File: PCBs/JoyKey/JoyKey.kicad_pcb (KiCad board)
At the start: 2 copper layers, 90.2 x 55 mm, 15 parts, among them J1 OLED_DISPLAY, SW2 SW_Push_45deg, SW3 SW_Push_45deg, SW4 SW_Push_45deg, SW5 SW_Push_45deg, U1 Seeed Studio XIAO RP2040

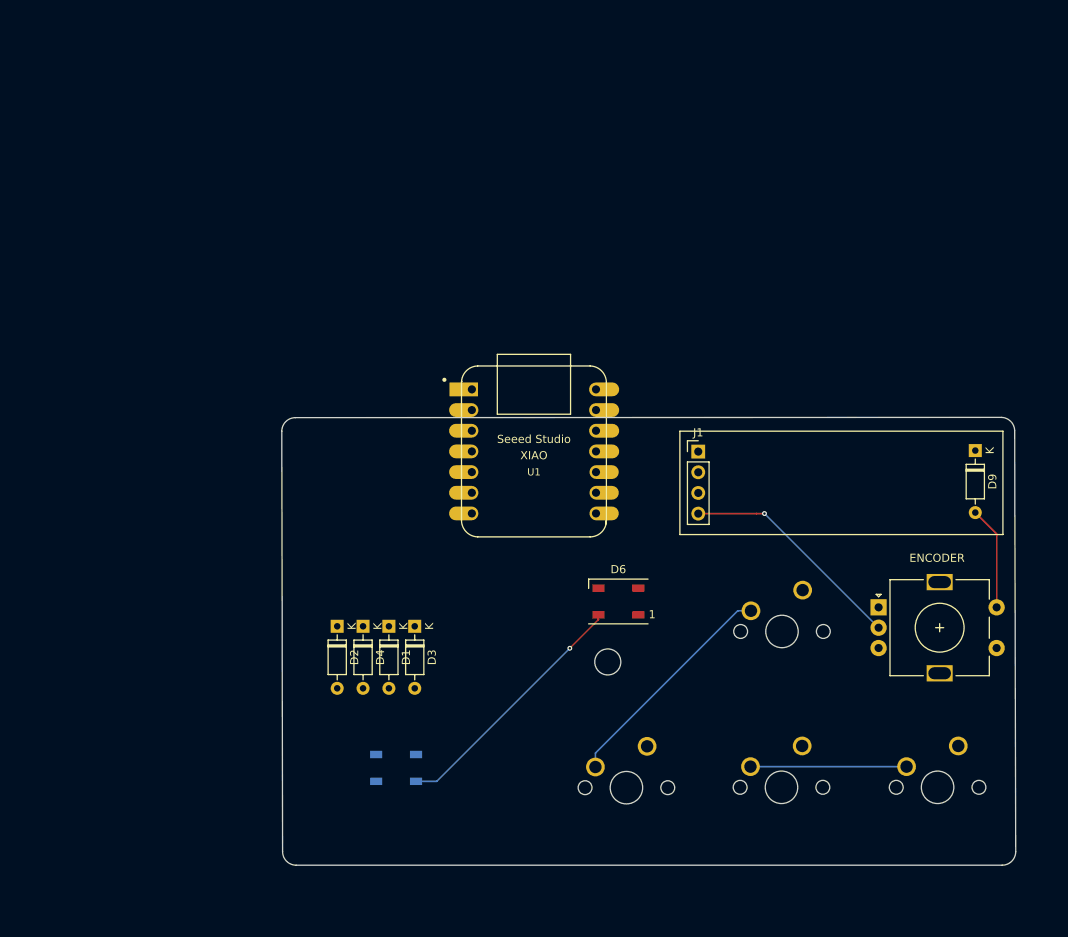
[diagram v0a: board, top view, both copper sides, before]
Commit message: Updated Parts in PCB
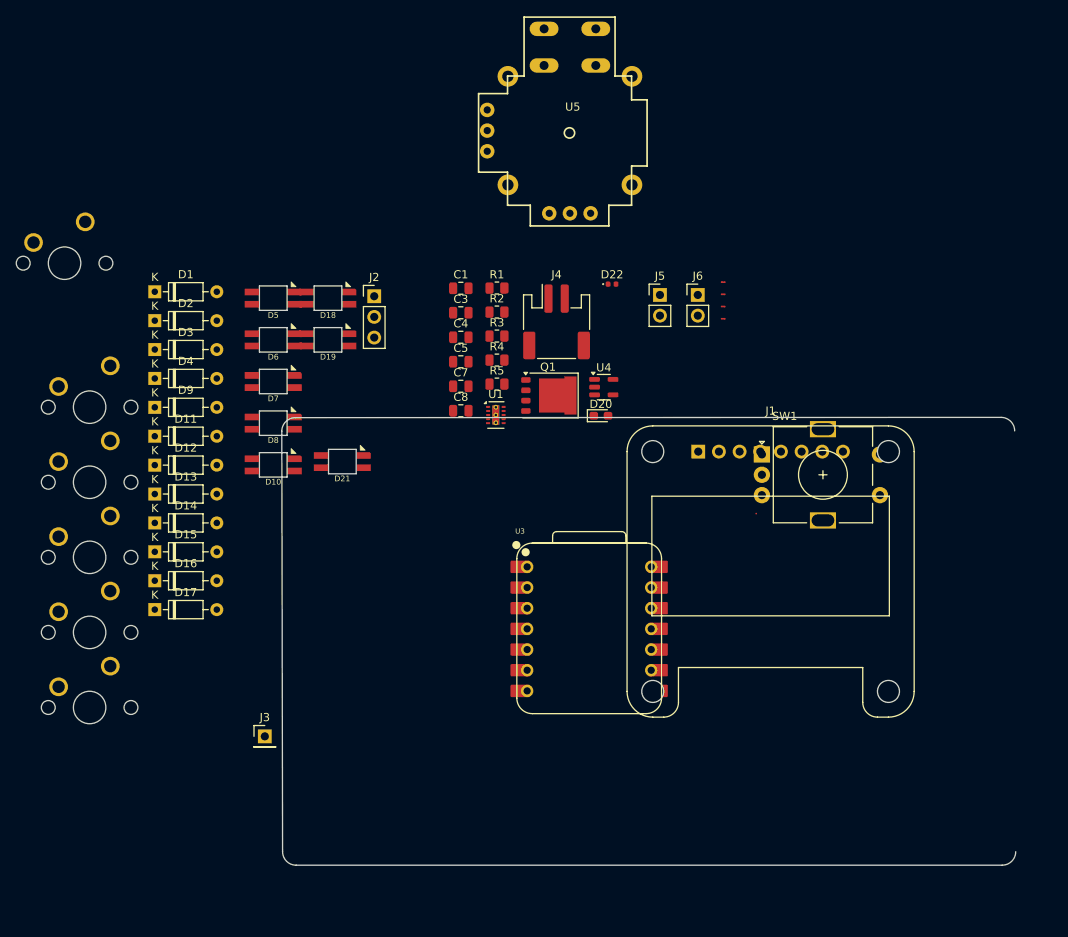
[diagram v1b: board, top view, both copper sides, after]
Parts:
- removed ENCODER: RotaryEncoder_Switch, Rotary_Encoder:RotaryEncoder_Alps_EC11E-Switch_Vertical_H20mm
- removed REF**: MountingHole_3.2mm_M3, MountingHole:MountingHole_3.2mm_M3
- added C1: 10uF, 16v, Capacitor_SMD:C_0805_2012Metric, F.Cu at (122.3, 58.2)
- added C3: 10uF, 16v, Capacitor_SMD:C_0805_2012Metric, F.Cu at (122.3, 61.2)
- added C4: 10uF, 16v, Capacitor_SMD:C_0805_2012Metric, F.Cu at (122.3, 64.2)
- added C5: 1uF, Capacitor_SMD:C_0805_2012Metric, F.Cu at (122.3, 67.2)
- added C7: 100nF, 16v, Capacitor_SMD:C_0805_2012Metric, F.Cu at (122.3, 70.2)
- added C8: 2.2uF, 10v, Capacitor_SMD:C_0805_2012Metric, F.Cu at (122.3, 73.2)
- added D10: SK6812MINI, SK6812MINI-E:SK6812MINI-E, F.Cu at (99.3, 79.9)
- added D11: D, Diode_THT:D_DO-35_SOD27_P7.62mm_Horizontal, F.Cu at (84.7, 76.3)
- added D12: D, Diode_THT:D_DO-35_SOD27_P7.62mm_Horizontal, F.Cu at (84.7, 79.9)
- added D13: D, Diode_THT:D_DO-35_SOD27_P7.62mm_Horizontal, F.Cu at (84.7, 83.4)
- added D14: D, Diode_THT:D_DO-35_SOD27_P7.62mm_Horizontal, F.Cu at (84.7, 87.0)
- added D15: D, Diode_THT:D_DO-35_SOD27_P7.62mm_Horizontal, F.Cu at (84.7, 90.5)
- added D16: D, Diode_THT:D_DO-35_SOD27_P7.62mm_Horizontal, F.Cu at (84.7, 94.1)
- added D17: D, Diode_THT:D_DO-35_SOD27_P7.62mm_Horizontal, F.Cu at (84.7, 97.6)
- added D18: SK6812MINI, SK6812MINI-E:SK6812MINI-E, F.Cu at (106.0, 59.4)
- added D19: SK6812MINI, SK6812MINI-E:SK6812MINI-E, F.Cu at (106.0, 64.5)
- added D20: Osram LT Q99G.01 green led, LED_SMD:LED_0603_1608Metric_Pad1.05x0.95mm_HandSolder, F.Cu at (139.6, 73.8)
- added D21: SK6812MINI, SK6812MINI-E:SK6812MINI-E, F.Cu at (107.8, 79.5)
- added D22: GSDH3005, Diode_SMD:D_0402_1005Metric, F.Cu at (140.9, 57.7)
- added D7: SK6812MINI, SK6812MINI-E:SK6812MINI-E, F.Cu at (99.3, 69.6)
- added D8: SK6812MINI, SK6812MINI-E:SK6812MINI-E, F.Cu at (99.3, 74.7)
- added J2: Conn_01x03_Socket, Connector_PinHeader_2.54mm:PinHeader_1x03_P2.54mm_Vertical, F.Cu at (111.7, 59.1)
- added J3: Testpad wire hole1, Connector_PinHeader_2.54mm:PinHeader_1x01_P2.54mm_Vertical, F.Cu at (98.3, 113.2)
- added J4: JST PH, Connector_JST:JST_PH_S2B-PH-SM4-TB_1x02-1MP_P2.00mm_Horizontal, F.Cu at (134.1, 62.3)
- added J5: Top Trigger 1, Connector_PinHeader_2.54mm:PinHeader_1x02_P2.54mm_Vertical, F.Cu at (146.8, 59.0)
- added J6: Top Trigger 2, Connector_PinHeader_2.54mm:PinHeader_1x02_P2.54mm_Vertical, F.Cu at (151.5, 59.0)
- added NT1: NetTie_2, custom_Connector:NetTie-2_SMD_Pad0.2mm, F.Cu at (154.6, 57.4)
- added NT2: NetTie_2, custom_Connector:NetTie-2_SMD_Pad0.2mm, F.Cu at (154.6, 58.9)
- added NT3: NetTie_2, custom_Connector:NetTie-2_SMD_Pad0.2mm, F.Cu at (154.6, 60.4)
- added NT4: NetTie_2, custom_Connector:NetTie-2_SMD_Pad0.2mm, F.Cu at (154.6, 61.9)
- added Q1: PMOS,Si7157DP, Package_DFN_QFN:PQFN-8-EP_6x5mm_P1.27mm_Generic, F.Cu at (133.1, 71.3)
- added R1: 402 ohm, Resistor_SMD:R_0805_2012Metric, F.Cu at (126.8, 58.1)
- added R2: 1k, Resistor_SMD:R_0805_2012Metric, F.Cu at (126.8, 61.1)
- added R3: 230ohm, Resistor_SMD:R_0805_2012Metric, F.Cu at (126.8, 64.0)
- added R4: 1k, Resistor_SMD:R_0805_2012Metric, F.Cu at (126.8, 67.0)
- added R5: 2k, Resistor_SMD:R_0805_2012Metric, F.Cu at (126.8, 69.9)
- added SW1: RotaryEncoder_Switch, Rotary_Encoder:RotaryEncoder_Alps_EC11E-Switch_Vertical_H20mm, F.Cu at (159.3, 78.6)
- added SW6: SW_Push_45deg, MX_Solderable:MX-Solderable-1U, F.Cu at (76.7, 100.4)
- added SW7: SW_Push_45deg, MX_Solderable:MX-Solderable-1U, F.Cu at (76.7, 109.7)
- added U3: XIAO-RP2040-DIP, SEEED_XIAO:XIAO-RP2040-DIP, F.Cu at (138.1, 100.0)
- added U4: LP2981-3.3, Package_TO_SOT_SMD:SOT-23-5, F.Cu at (139.9, 70.3)
- added U5: 2_axis_analog_joystick_button, custom_Interface_HID:Adafruit 2-Axis joystick, F.Cu at (135.7, 39.1)
- D5: value WS2812B -> SK6812MINI; footprint LED_SMD:LED_WS2812B_PLCC4_5.0x5.0mm_P3.2mm -> SK6812MINI-E:SK6812MINI-E; moved to F.Cu
- D6: value WS2812B -> SK6812MINI; footprint LED_SMD:LED_WS2812B_PLCC4_5.0x5.0mm_P3.2mm -> SK6812MINI-E:SK6812MINI-E
- J1: footprint Connector_PinHeader_2.54mm:PinHeader_1x04_P2.54mm_Vertical -> Display:Adafruit_SSD1306
- U1: value Seeed Studio XIAO RP2040 -> BQ25060; footprint Seeed Studio XIAO Series Library:XIAO-Generic-Hybrid-14P-2.54-21X17.8MM -> custom_Power:WSON-10-1EP_2x3mm_P0.5mm_EP0.84x2.4mm_ThermalVias_0.3mm
- moved SW5 107.9 mm to (76.7, 91.2)
- moved D9 100.9 mm to (84.7, 72.8), turned to 0 degrees
- moved SW2 99.1 mm to (73.7, 55.1)
- moved SW4 92.9 mm to (76.7, 82.0)
- moved SW3 80.8 mm to (76.7, 72.8)
- moved D5 59.7 mm to (99.3, 59.4), turned to 0 degrees
- moved D6 53.2 mm to (99.3, 64.5), turned to 0 degrees
- moved D1 50.2 mm to (84.7, 58.6), turned to 0 degrees
- moved D3 46.6 mm to (84.7, 65.7), turned to 0 degrees
- moved D2 43.7 mm to (84.7, 62.1), turned to 0 degrees
- moved D4 39.8 mm to (84.7, 69.2), turned to 0 degrees
- moved U1 6.47 mm to (126.6, 73.7)
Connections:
- D1 pad 1: ROW0 -> /ROW0
- D2 pad 1: ROW0 -> /ROW0
- D3 pad 1: ROW1 -> /ROW0
- D4 pad 1: ROW1 -> /ROW1
- D5 pad 1: VCC -> Net-(D5-DOUT)
- D5 pad 2: Net-(D5-DOUT) -> GND
- D5 pad 3: GND -> Net-(D21-DOUT)
- D5 pad 4: WS2812B -> +3V3
- D6 pad 1: VCC -> Net-(D6-DOUT)
- D6 pad 2: unconnected-(D6-DOUT-Pad2) -> GND
- D6 pad 3: GND -> Net-(D5-DOUT)
- D6 pad 4: Net-(D5-DOUT) -> +3V3
- D9 pad 1: ROW0 -> /ROW1
- D9 pad 2: EC11SWA -> Net-(D9-A)
- J1 pad 3: VCC -> +3V3
- SW2 pad 1: COL0 -> /COL0
- SW3 pad 1: COL0 -> /COL1
- SW3 pad 2: Net-(D3-A) -> Net-(D2-A)
- SW4 pad 1: COL1 -> /COL0
- SW5 pad 1: COL1 -> /COL1
- SW5 pad 2: Net-(D2-A) -> Net-(D9-A)
- U1 pad 1: COL1 -> VCC
- U1 pad 10: COL2 -> Net-(U1-OUT)
- U1 pad 11: WS2812B -> GND
- U1 pad 2: COL0 -> Net-(U1-ISET)
- U1 pad 3: ROW1 -> GND
- U1 pad 4: ROW0 -> /Battery Management/LDO 4.9v
- U1 pad 5: SDA -> Net-(U1-TS)
- U1 pad 6: SCL -> /Battery Management/BATT+
- U1 pad 7: unconnected-(U1-PB08_A6_D6_TX-Pad7) -> GND
- U1 pad 8: EC11B -> /Battery Management/~{CHG}
- U1 pad 9: EC11A -> Net-(Q1-G)
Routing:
- net Net-(D5-DOUT): track 31.2 -> 0.00 mm, vias 1 -> 0
- net COL0: track 28.1 -> 0.00 mm
- net GND: track 28.0 -> 0.01 mm, vias 1 -> 0
- net COL1: track 19.2 -> 0.00 mm
- net EC11SWA: track 12.8 -> 0.00 mm
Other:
- board text added: "5.08 LED offset from key center"

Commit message: Started pcb placement
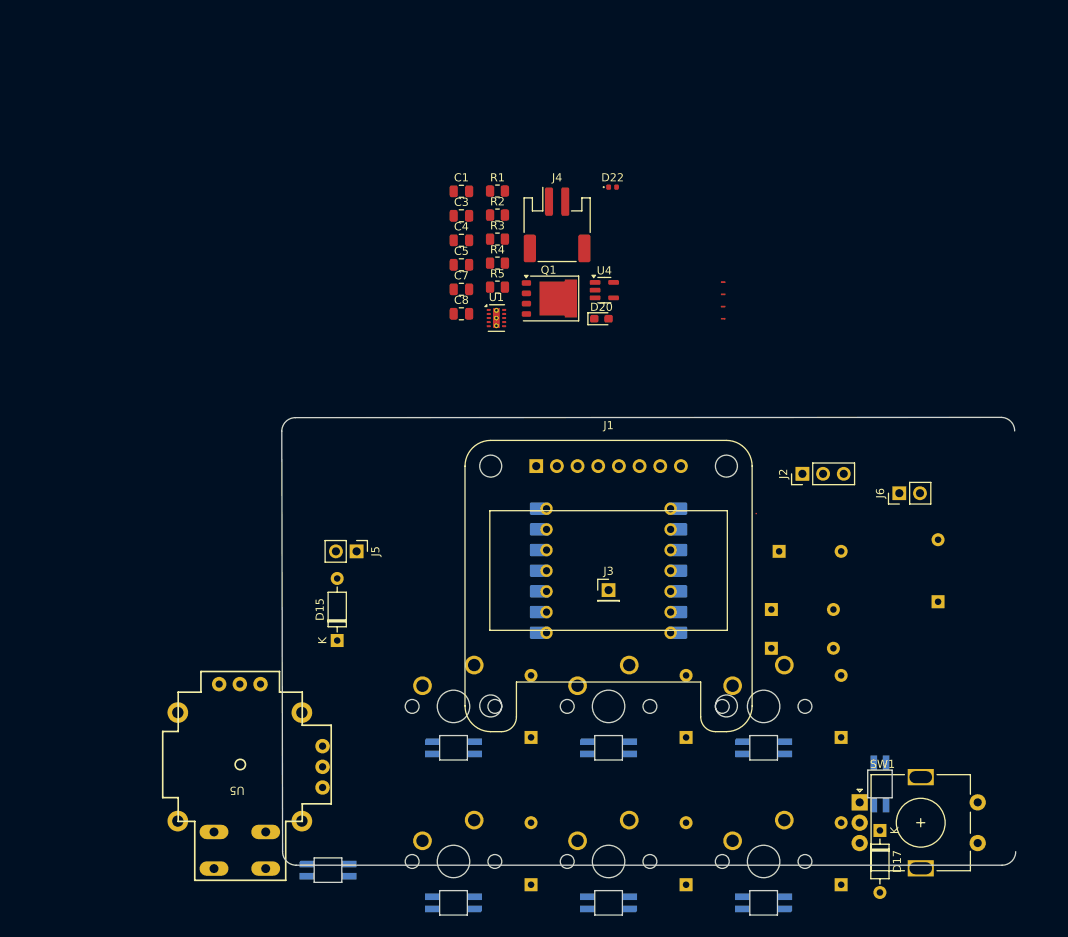
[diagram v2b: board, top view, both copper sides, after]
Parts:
- D1, D10, D11, D12, D13, D14, D16, D18, D19, D2, D21, D3, D4, D5, D6, D7, D8, D9, U3: moved to B.Cu
- moved D11 100.7 mm to (169.1, 131.4), turned to 90 degrees
- moved D3 96.9 mm to (169.1, 113.3), turned to 90 degrees
- moved D16 96.3 mm to (181.0, 96.7), turned to 90 degrees
- moved D17 93.1 mm to (173.8, 124.8), turned to -90 degrees
- moved D7 87.9 mm to (159.5, 133.7)
- moved D9 87.8 mm to (150.0, 131.4), turned to 90 degrees
- moved U5 87.5 mm to (95.2, 116.7), turned to 180 degrees
- moved SW6 87.5 mm to (159.5, 128.6)
- moved D19 87.0 mm to (173.8, 119.1), turned to -90 degrees
- moved D2 83.0 mm to (150.0, 113.3), turned to 90 degrees
- moved SW7 82.8 mm to (159.5, 109.5)
- moved D6 78.4 mm to (159.5, 114.6), turned to 180 degrees
- moved D4 77.5 mm to (131.0, 131.4), turned to 90 degrees
- moved D12 77.4 mm to (161.4, 90.5)
- moved D14 77.3 mm to (160.5, 102.4)
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
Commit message: Updated PCB components
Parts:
- moved D19 4.44 mm to (174.3, 114.7)
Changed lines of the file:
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@@
 	(footprint "SK6812MINI-E:SK6812MINI-E"
 		(layer "B.Cu")
-		(at 173.83125 119.0625 -90)
+		(at 174.3 114.65 -90)
 		(property "Reference" "D19"
 			(at 0 -2.1 90)

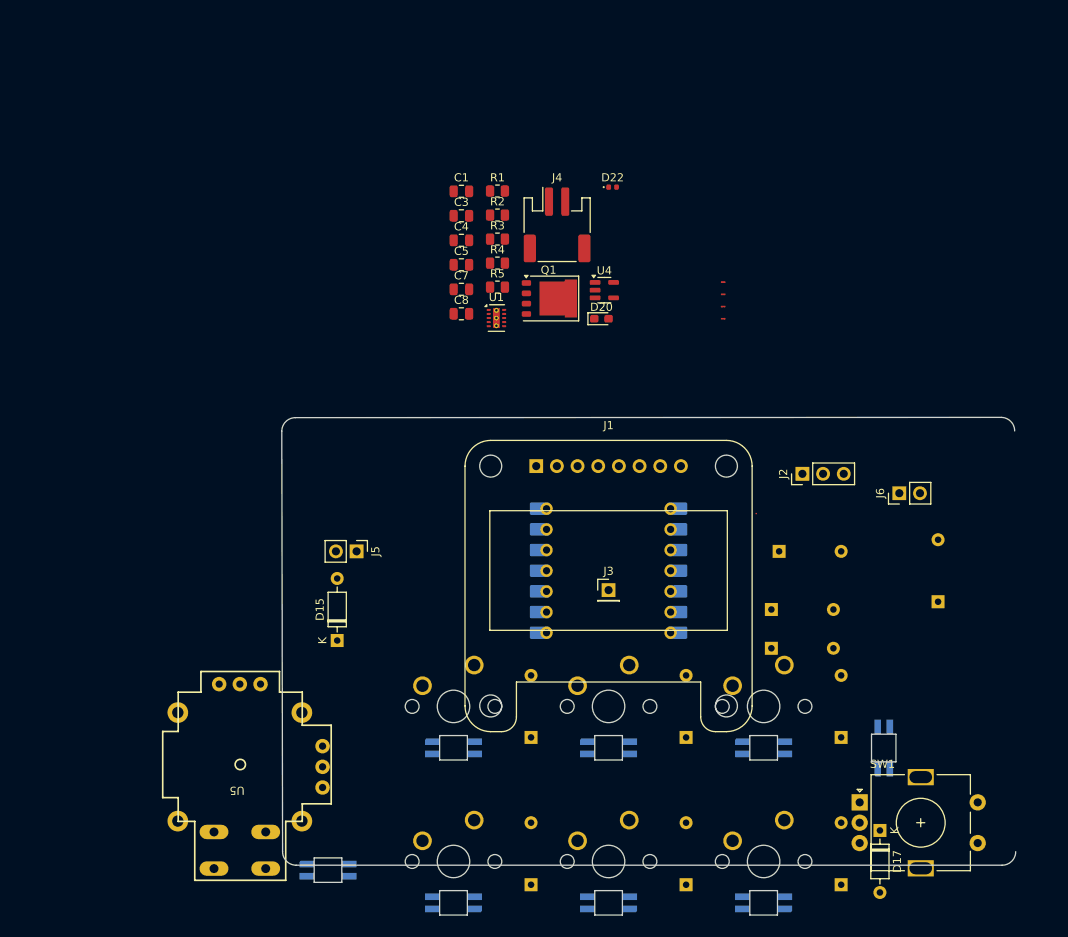
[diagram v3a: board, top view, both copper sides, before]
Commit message: Updated display to proper one
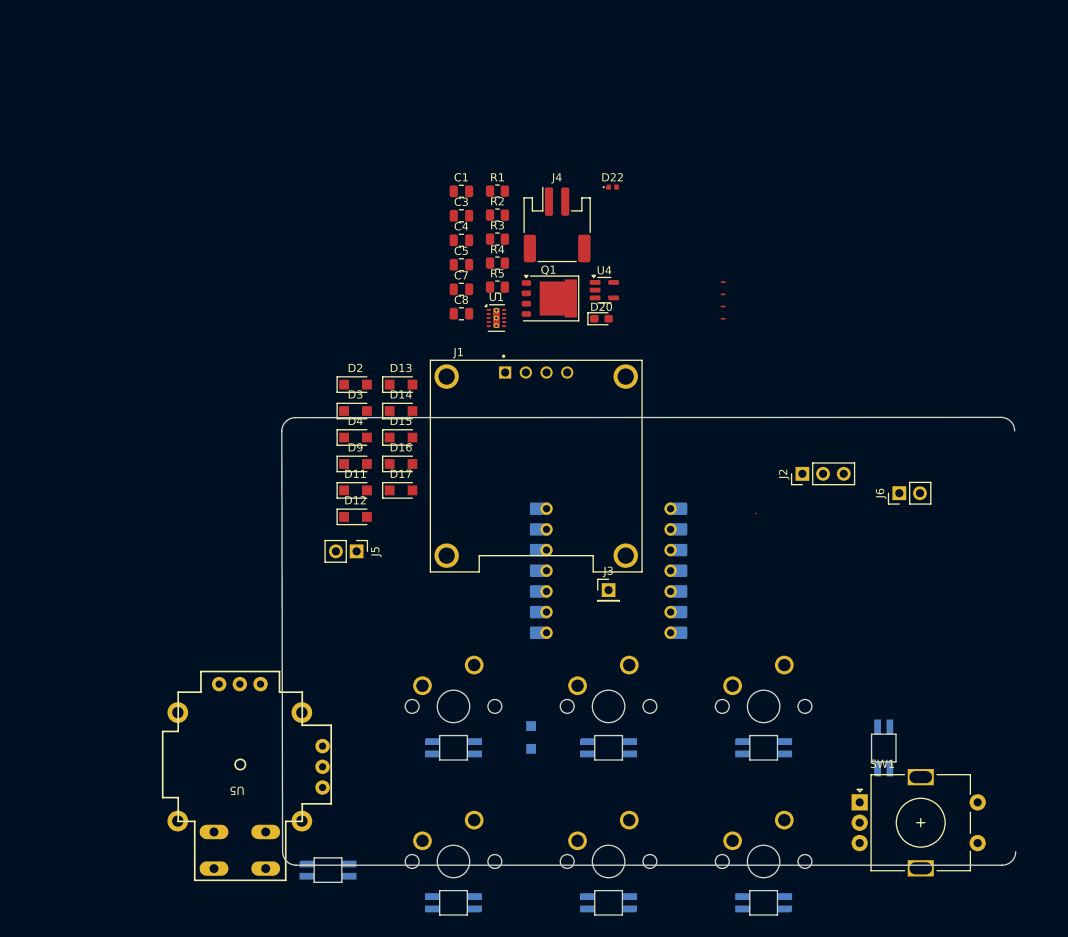
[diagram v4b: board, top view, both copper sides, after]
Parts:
- D1, D15, D17: value D -> 1N4148W; footprint Diode_THT:D_DO-35_SOD27_P7.62mm_Horizontal -> Diode_SMD:Nexperia_CFP3_SOD-123W
- D11, D12, D13, D14, D16, D2, D3, D4, D9: value D -> 1N4148W; footprint Diode_THT:D_DO-35_SOD27_P7.62mm_Horizontal -> Diode_SMD:Nexperia_CFP3_SOD-123W; moved to F.Cu
- J1: footprint Display:Adafruit_SSD1306 -> SSD1306:SSD1306-OLED096-128x64
- moved D11 76.9 mm to (109.4, 83.0), turned to 0 degrees
- moved D17 72.2 mm to (115.0, 83.0), turned to 0 degrees
- moved D3 71.9 mm to (109.4, 73.2), turned to 0 degrees
- moved D16 68.1 mm to (115.0, 79.8), turned to 0 degrees
- moved D9 65.7 mm to (109.4, 79.8), turned to 0 degrees
- moved D2 59.4 mm to (109.4, 70.0), turned to 0 degrees
- moved D4 59.0 mm to (109.4, 76.5), turned to 0 degrees
- moved D14 54.0 mm to (115.0, 73.2)
- moved D13 53.2 mm to (115.0, 70.0)
- moved D12 52.2 mm to (109.4, 86.2)
- moved D15 26.1 mm to (115.0, 76.5), turned to 0 degrees
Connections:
- D12 pad 1: /ROW2 -> /ROW1
- D12 pad 2: /Analog Input/EC11A -> Net-(D12-A)
- D13 pad 1: /ROW2 -> /ROW1
- D13 pad 2: /Analog Input/EC11B -> Net-(D13-A)
- D14 pad 2: /Analog Input/EC11SWB -> /Analog Input/EC11A
- D15 pad 1: /ROW0 -> /ROW2
- D15 pad 2: Net-(D15-A) -> /Analog Input/EC11B
- D16 pad 1: /ROW1 -> /ROW2
- D16 pad 2: Net-(D16-A) -> /Analog Input/EC11SWB
- D18 pad 4: VCC -> +3V3
- D19 pad 4: VCC -> +3V3
- D4 pad 1: /ROW1 -> /ROW0
- J1 pad 1: SDA -> GND
- J1 pad 2: SCL -> +3V3
- J1 pad 3: +3V3 -> SCL
- J1 pad 4: GND -> SDA
- J2 pad 1: VCC -> +3V3
- J5 pad 2: Net-(D15-A) -> Net-(D4-A)
- J6 pad 2: Net-(D16-A) -> Net-(D13-A)
- SW4 pad 2: Net-(D4-A) -> Net-(D9-A)
- SW5 pad 2: Net-(D9-A) -> Net-(D11-A)
- SW6 pad 2: Net-(D11-A) -> Net-(D12-A)
- U5 pad MP: (no net) -> GND

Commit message: Finished main part layout
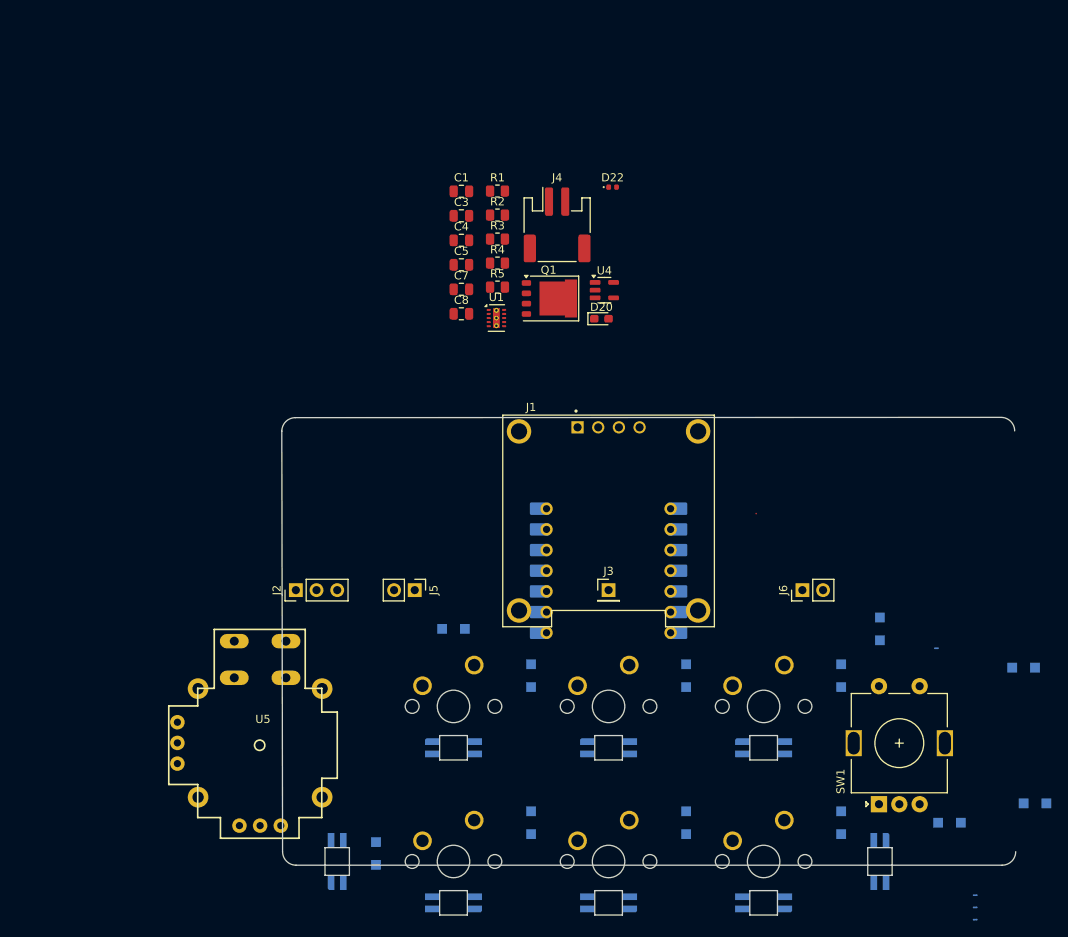
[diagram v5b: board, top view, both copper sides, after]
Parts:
- D11, D12, D13, D14, D15, D16, D17, D2, D3, D4, D9, NT1, NT2, NT3, NT4: moved to B.Cu
- moved D14 91.6 mm to (192.9, 121.4), turned to 180 degrees
- moved D15 82.3 mm to (182.4, 123.8), turned to 180 degrees
- moved D16 80.5 mm to (191.5, 104.8), turned to 180 degrees
- moved NT2 80.0 mm to (185.5, 132.7), turned to 180 degrees
- moved NT3 80.0 mm to (185.5, 134.2), turned to 180 degrees
- moved NT4 80.0 mm to (185.5, 135.7), turned to 180 degrees
- moved D12 70.5 mm to (169.1, 123.8), turned to 90 degrees
- moved D19 68.6 mm to (107.2, 128.6)
- moved D3 67.9 mm to (169.1, 105.8), turned to 90 degrees
- moved D13 66.0 mm to (173.8, 100.0), turned to 90 degrees
- moved J2 63.8 mm to (102.1, 95.2)
- moved D11 57.6 mm to (150.0, 123.8), turned to 90 degrees
- moved D2 54.1 mm to (150.0, 105.8), turned to 90 degrees
- moved NT1 52.1 mm to (180.8, 102.4), turned to 180 degrees
- moved D9 49.1 mm to (131.0, 123.8), turned to 90 degrees
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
